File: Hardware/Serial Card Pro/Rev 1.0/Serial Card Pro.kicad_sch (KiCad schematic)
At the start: 27 parts, among them J1 6502 Card Edge, J2 DB9 Male (DTE), J3 Conn_02x08_Odd_Even, J4 DCD Select, U1 MAX232, U2 MAX232, U3 74HC138, U4 6551, Y1 1.8432 Mhz

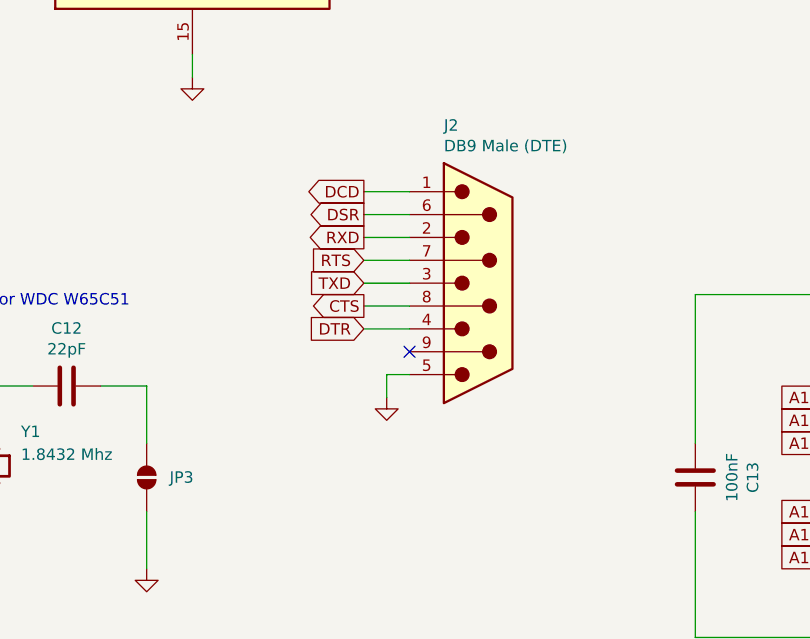
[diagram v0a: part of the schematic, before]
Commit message: Fix DB Connectors
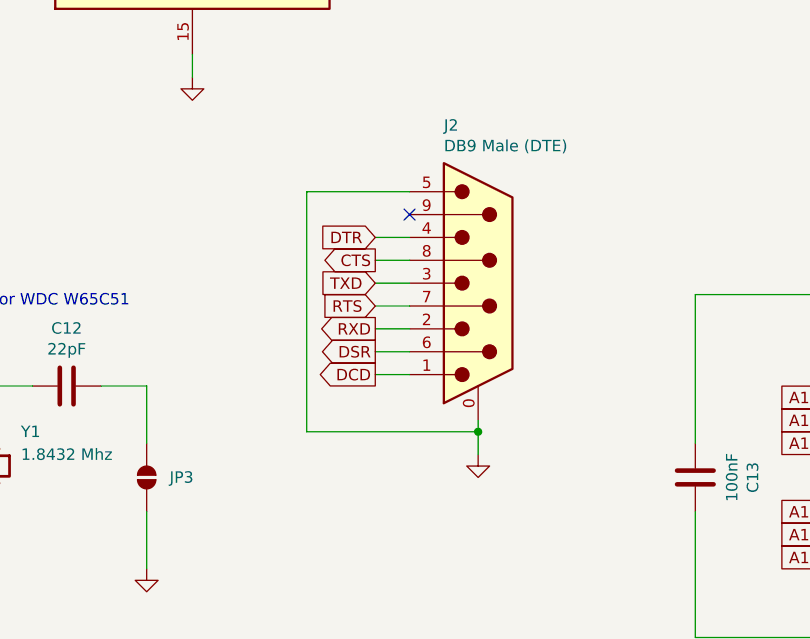
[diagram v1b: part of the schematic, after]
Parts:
- J2: footprint 6502 Parts:DB9 Male -> Connector_Dsub:DSUB-9_Pins_Horizontal_P2.77x2.84mm_EdgePinOffset7.70mm_Housed_MountingHolesOffset9.12mm; symbol 6502 Parts:DB9 Male -> Connector:DE9_Pins_MountingHoles; now in the parts list
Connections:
- net GND: now also J2.0 (PAD)

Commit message: More parts cleanup
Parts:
- J2: Digikey (none) -> 609-1481-ND; MPN (none) -> D09P33E4GX00LF; Sparkfun PRT-00429 -> (none)
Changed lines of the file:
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@@
 			)
 		)
-		(property "Sparkfun" "PRT-00429"
+		(property "Digikey" "609-1481-ND"
 			(at 158.75 124.46 0)
 			(effects
+				(font
+					(size 1.27 1.27)
+				)
+				(hide yes)
+			)
+		)
+		(property "MPN" "D09P33E4GX00LF"
+			(at 158.75 124.46 0)
+			(effects

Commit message: Cleanup for production
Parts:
- J2: value DB9 Male (DTE) -> DB9 MALE (DTE)
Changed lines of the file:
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@@
 			)
 		)
-		(property "Value" "DB9 Male (DTE)"
+		(property "Value" "DB9 MALE (DTE)"
 			(at 154.94 109.22 0)
 			(effects
